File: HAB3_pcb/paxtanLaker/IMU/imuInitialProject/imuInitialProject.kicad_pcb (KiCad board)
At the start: 2 copper layers, 12 parts, among them J1 Conn_01x09_Female, J2 Conn_01x02_Female, U1 LSM9DS0

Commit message: started tracing
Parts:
- moved C3 20.4 mm to (167.6, 88.6)
- moved U1 19.2 mm to (166.4, 83.8)
- moved C1 19.2 mm to (171.4, 81.3)
- moved R2 19.2 mm to (171.4, 85.1)
- moved C2 19.2 mm to (171.4, 82.5)
- moved R4 19.2 mm to (171.4, 83.8)
- moved J2 16.7 mm to (160.0, 69.8)
- moved D1 14.5 mm to (151.1, 69.8)
- moved D2 14.5 mm to (151.1, 68.6)
- moved R1 14.5 mm to (151.1, 67.3)
- moved R3 14.5 mm to (151.1, 71.1)
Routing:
- net Net-(C1-Pad1): track 0.00 -> 38.1 mm
- net Net-(J1-Pad9): track 0.00 -> 36.8 mm
- net Net-(J1-Pad8): track 0.00 -> 30.3 mm
- net Net-(C1-Pad2): track 0.00 -> 23.7 mm
- net Net-(C3-Pad2): track 0.00 -> 4.95 mm
- net Net-(C3-Pad1): track 0.00 -> 4.50 mm
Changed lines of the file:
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@@
   (general
     (thickness 1.6)
-    (drawings 4)
-    (tracks 0)
+    (drawings 6)
+    (tracks 49)
     (zones 0)
     (modules 12)
@@
   )
   (module Capacitor_SMD:C_0402_1005Metric (layer F.Cu)
-    (at 152.4 78.74)
+    (at 171.45 81.28)
     (descr "Capacitor SMD 0402 (1005 Metric), square (rectangular) end terminal, IPC_7351 nominal, (Body size source: http://www.tortai-tech.com/upload/download/2011102023233369053.pdf), generated with kicad-footprint-generator")
     (tags capacitor)
@@
   )
   (module Capacitor_SMD:C_0402_1005Metric (layer F.Cu)
-    (at 152.4 80.01)
+    (at 171.45 82.55)
     (descr "Capacitor SMD 0402 (1005 Metric), square (rectangular) end terminal, IPC_7351 nominal, (Body size source: http://www.tortai-tech.com/upload/download/2011102023233369053.pdf), generated with kicad-footprint-generator")
     (tags capacitor)
@@
   )
   (module Capacitor_SMD:C_0402_1005Metric (layer F.Cu)
-    (at 147.32 86.36)
+    (at 167.64 88.646)
     (descr "Capacitor SMD 0402 (1005 Metric), square (rectangular) end terminal, IPC_7351 nominal, (Body size source: http://www.tortai-tech.com/upload/download/2011102023233369053.pdf), generated with kicad-footprint-generator")
     (tags capacitor)
@@
   )
   (module Diode_SMD:D_0402_1005Metric (layer F.Cu)
-    (at 142.24 81.28)
+    (at 151.13 69.85)
     (descr "Diode SMD 0402 (1005 Metric), square (rectangular) end terminal, IPC_7351 nominal, (Body size source: http://www.tortai-tech.com/upload/download/2011102023233369053.pdf), generated with kicad-footprint-generator")
     (tags diode)
@@
   )
   (module Diode_SMD:D_0402_1005Metric (layer F.Cu)
-    (at 142.24 80.01)
+    (at 151.13 68.58)
     (descr "Diode SMD 0402 (1005 Metric), square (rectangular) end terminal, IPC_7351 nominal, (Body size source: http://www.tortai-tech.com/upload/download/2011102023233369053.pdf), generated with kicad-footprint-generator")
     (tags diode)
@@
   )
   (module Resistor_SMD:R_0402_1005Metric (layer F.Cu)
-    (at 142.24 78.74)
+    (at 151.13 67.31)
     (descr "Resistor SMD 0402 (1005 Metric), square (rectangular) end terminal, IPC_7351 nominal, (Body size source: http://www.tortai-tech.com/upload/download/2011102023233369053.pdf), generated with kicad-footprint-generator")
     (tags resistor)
@@
   )
   (module Resistor_SMD:R_0402_1005Metric (layer F.Cu)
-    (at 152.4 82.55)
+    (at 171.45 85.09)
     (descr "Resistor SMD 0402 (1005 Metric), square (rectangular) end terminal, IPC_7351 nominal, (Body size source: http://www.tortai-tech.com/upload/download/2011102023233369053.pdf), generated with kicad-footprint-generator")
     (tags resistor)
@@
   )
   (module Resistor_SMD:R_0402_1005Metric (layer F.Cu)
-    (at 142.24 82.55)
+    (at 151.13 71.12)
     (descr "Resistor SMD 0402 (1005 Metric), square (rectangular) end terminal, IPC_7351 nominal, (Body size source: http://www.tortai-tech.com/upload/download/2011102023233369053.pdf), generated with kicad-footprint-generator")
     (tags resistor)
@@
   )
   (module Resistor_SMD:R_0402_1005Metric (layer F.Cu)
-    (at 152.4 81.28)
+    (at 171.45 83.82)
     (descr "Resistor SMD 0402 (1005 Metric), square (rectangular) end terminal, IPC_7351 nominal, (Body size source: http://www.tortai-tech.com/upload/download/2011102023233369053.pdf), generated with kicad-footprint-generator")
     (tags resistor)
@@
   )
   (module LSM9DS04:LGA-24LSM (layer F.Cu)
-    (at 147.32 81.28)
+    (at 166.37 83.82)
     (descr "<h3>LGA 4x4x1 mm 24-lead</h3><ul><li>0.5mm pitch</li><li>Pads are 0.35x0.2 mm square</li></ul><p>This package is used for:<p><ul><li>ST Micro LSM9DS0 3D accel/gyro/mag</li></ul>")
     (attr smd)
@@
   )
   (module Connector_PinHeader_2.54mm:PinHeader_1x02_P2.54mm_Horizontal (layer F.Cu)
-    (at 143.51 67.31)
+    (at 160.02 69.85)
     (descr "Through hole angled pin header, 1x02, 2.54mm pitch, 6mm pin length, single row")
     (tags "Through hole angled pin header THT 1x02 2.54mm single row")
@@
     (fp_line (start 10.55 4.35) (end 10.55 -1.8) (layer F.CrtYd) (width 0.05))
     (fp_line (start 10.55 -1.8) (end -1.8 -1.8) (layer F.CrtYd) (width 0.05))
-    (fp_text user %R (at 2.77 1.27 90) (layer F.Fab)
+    (fp_text user %R (at 2.54 1.27 90) (layer F.Fab)
       (effects (font (size 1 1) (thickness 0.15)))
     )
@@
     )
   )
+  (gr_line (start 176.53 64.77) (end 154.94 64.77) (angle 90) (layer F.Adhes) (width 0.2))
+  (gr_line (start 176.53 91.44) (end 176.53 64.77) (angle 90) (layer F.Adhes) (width 0.2))
+  (gr_line (start 154.94 91.44) (end 176.53 91.44) (angle 90) (layer F.Adhes) (width 0.2))
   (gr_line (start 154.94 64.77) (end 127 64.77) (angle 90) (layer F.Adhes) (width 0.2))
-  (gr_line (start 154.94 91.44) (end 154.94 64.77) (angle 90) (layer F.Adhes) (width 0.2))
   (gr_line (start 127 91.44) (end 154.94 91.44) (angle 90) (layer F.Adhes) (width 0.2))
   (gr_line (start 127 64.77) (end 127 91.44) (angle 90) (layer F.Adhes) (width 0.2))
+  (segment (start 167.155 88.646) (end 165.608 88.646) (width 0.25) (layer F.Cu) (net 1) (status 400000))
+  (segment (start 165.62 88.634) (end 165.62 85.695) (width 0.25) (layer F.Cu) (net 1) (status 800000))
+  (segment (start 165.608 88.646) (end 165.62 88.634) (width 0.25) (layer F.Cu) (net 1))
+  (segment (start 168.125 88.646) (end 168.125 87.907) (width 0.25) (layer F.Cu) (net 2) (status 400000))
+  (segment (start 166.12 87.88) (end 166.12 85.695) (width 0.25) (layer F.Cu) (net 2) (status 800000))
+  (segment (start 166.116 87.884) (end 166.12 87.88) (width 0.25) (layer F.Cu) (net 2))
+  (segment (start 168.102 87.884) (end 166.116 87.884) (width 0.25) (layer F.Cu) (net 2))
+  (segment (start 168.125 87.907) (end 168.102 87.884) (width 0.25) (layer F.Cu) (net 2))
+  (segment (start 138.685001 85.595001) (end 141.221001 85.595001) (width 0.25) (layer B.Cu) (net 12) (status 400000))
+  (segment (start 167.132 87.122) (end 167.132 85.852) (width 0.25) (layer B.Cu) (net 12))
+  (segment (start 142.748 87.122) (end 167.132 87.122) (width 0.25) (layer B.Cu) (net 12))
+  (segment (start 141.221001 85.595001) (end 142.748 87.122) (width 0.25) (layer B.Cu) (net 12))
+  (segment (start 166.62 85.695) (end 166.62 87.372) (width 0.25) (layer F.Cu) (net 13) (status 400000))
+  (segment (start 163.319001 88.135001) (end 138.685001 88.135001) (width 0.25) (layer F.Cu) (net 13) (status 800000))
+  (segment (start 164.592 89.408) (end 163.319001 88.135001) (width 0.25) (layer F.Cu) (net 13))
+  (segment (start 168.91 89.408) (end 164.592 89.408) (width 0.25) (layer F.Cu) (net 13))
+  (segment (start 168.91 87.376) (end 168.91 89.408) (width 0.25) (layer F.Cu) (net 13))
+  (segment (start 166.62 87.372) (end 166.624 87.376) (width 0.25) (layer F.Cu) (net 13))
+  (segment (start 166.624 87.376) (end 168.91 87.376) (width 0.25) (layer F.Cu) (net 13))
+  (segment (start 160.02 72.39) (end 157.226 72.39) (width 0.25) (layer B.Cu) (net 16) (status 400000))
+  (segment (start 164.592 86.36) (end 165.1 85.852) (width 0.25) (layer B.Cu) (net 16))
+  (segment (start 162.306 86.36) (end 164.592 86.36) (width 0.25) (layer B.Cu) (net 16))
+  (segment (start 161.798 85.852) (end 162.306 86.36) (width 0.25) (layer B.Cu) (net 16))
+  (segment (start 161.798 80.518) (end 161.798 82.55) (width 0.25) (layer B.Cu) (net 16))
+  (segment (start 161.798 82.55) (end 161.798 83.058) (width 0.25) (layer B.Cu) (net 16))
+  (segment (start 161.798 83.058) (end 161.798 83.312) (width 0.25) (layer B.Cu) (net 16))
+  (segment (start 161.798 83.312) (end 161.798 83.566) (width 0.25) (layer B.Cu) (net 16))
+  (segment (start 161.798 83.566) (end 161.798 83.82) (width 0.25) (layer B.Cu) (net 16))
+  (segment (start 161.798 83.82) (end 161.798 84.074) (width 0.25) (layer B.Cu) (net 16))
+  (segment (start 161.798 84.074) (end 161.798 84.582) (width 0.25) (layer B.Cu) (net 16))
+  (segment (start 161.798 84.582) (end 161.798 85.09) (width 0.25) (layer B.Cu) (net 16))
+  (segment (start 161.798 85.09) (end 161.798 85.852) (width 0.25) (layer B.Cu) (net 16))
+  (segment (start 157.226 75.946) (end 161.798 80.518) (width 0.25) (layer B.Cu) (net 16))
+  (segment (start 157.226 72.39) (end 157.226 75.946) (width 0.25) (layer B.Cu) (net 16))
+  (segment (start 161.798 85.09) (end 164.338 85.09) (width 0.25) (layer B.Cu) (net 16))
+  (segment (start 161.798 84.582) (end 164.592 84.582) (width 0.25) (layer B.Cu) (net 16))
+  (segment (start 161.798 84.074) (end 164.592 84.074) (width 0.25) (layer B.Cu) (net 16))
+  (segment (start 161.798 83.566) (end 164.338 83.566) (width 0.25) (layer B.Cu) (net 16))
+  (segment (start 161.798 83.058) (end 164.592 83.058) (width 0.25) (layer B.Cu) (net 16))
+  (segment (start 161.798 82.55) (end 164.592 82.55) (width 0.25) (layer B.Cu) (net 16))
+  (segment (start 160.02 69.85) (end 156.718 69.85) (width 0.25) (layer B.Cu) (net 17) (status 400000))
+  (segment (start 148.336 67.31) (end 150.622 67.31) (width 0.25) (layer B.Cu) (net 17))
+  (segment (start 148.336 65.786) (end 148.336 67.31) (width 0.25) (layer B.Cu) (net 17))
+  (segment (start 153.67 65.786) (end 148.336 65.786) (width 0.25) (layer B.Cu) (net 17))
+  (segment (start 156.718 69.85) (end 153.67 66.802) (width 0.25) (layer B.Cu) (net 17))
+  (segment (start 153.67 66.802) (end 153.67 65.786) (width 0.25) (layer B.Cu) (net 17))
+  (segment (start 148.336 67.31) (end 148.336 70.866) (width 0.25) (layer B.Cu) (net 17))
+  (segment (start 148.59 71.12) (end 150.622 71.12) (width 0.25) (layer B.Cu) (net 17))
+  (segment (start 148.336 70.866) (end 148.59 71.12) (width 0.25) (layer B.Cu) (net 17))
 )

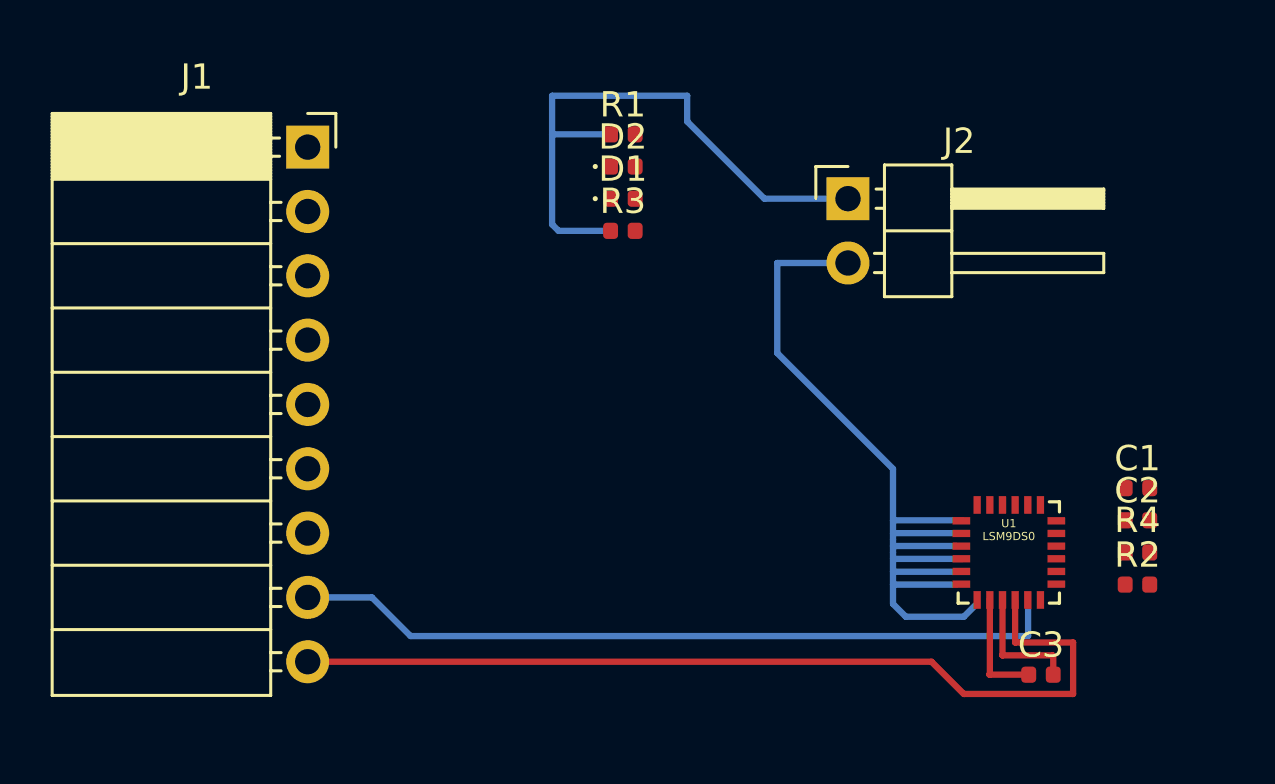
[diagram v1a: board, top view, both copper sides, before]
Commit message: Final PCB IMU
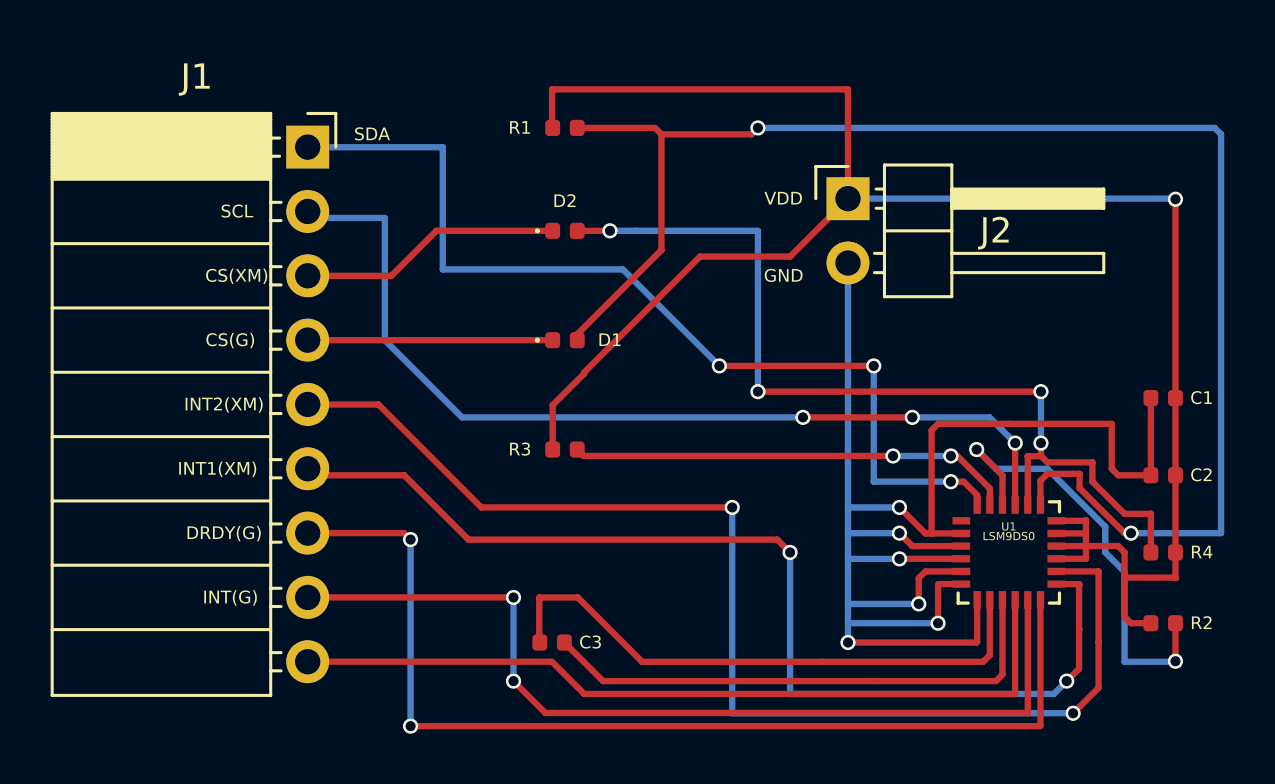
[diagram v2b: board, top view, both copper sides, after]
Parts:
- moved C3 19.3 mm to (148.3, 87.4)
- moved R3 8.93 mm to (148.8, 79.8)
- moved D1 6.04 mm to (148.8, 75.4)
- moved C1 3.70 mm to (172.5, 77.7)
- moved D2 3.42 mm to (148.8, 71.1)
- moved R1 2.30 mm to (148.8, 67.1)
- moved C2 2.05 mm to (172.5, 80.8)
- moved R2 1.83 mm to (172.5, 86.6)
- moved R4 1.02 mm to (172.5, 83.8)
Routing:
- net Net-(D1-Pad2): track 0.00 -> 60.5 mm, vias 0 -> 2
- net Net-(C1-Pad2): track 23.7 -> 75.9 mm, vias 0 -> 1
- net Net-(J1-Pad5): track 0.00 -> 47.8 mm, vias 0 -> 2
- net Net-(J1-Pad6): track 0.00 -> 42.1 mm, vias 0 -> 2
- net Net-(J1-Pad7): track 0.00 -> 41.4 mm, vias 0 -> 2
- net Net-(J1-Pad1): track 0.00 -> 38.0 mm, vias 0 -> 3
- net Net-(J1-Pad2): track 0.00 -> 37.0 mm, vias 0 -> 3
- net Net-(D2-Pad2): track 0.00 -> 37.0 mm, vias 0 -> 4
- net Net-(C1-Pad1): track 38.1 -> 65.2 mm, vias 0 -> 6
- net Net-(C3-Pad1): track 4.50 -> 22.9 mm
- net Net-(R2-Pad2): track 0.00 -> 18.2 mm, vias 0 -> 2
- net Net-(R3-Pad2): track 0.00 -> 17.6 mm, vias 0 -> 2
- net Net-(C3-Pad2): track 4.95 -> 21.0 mm
- net Net-(D2-Pad1): track 0.00 -> 10.4 mm
- net Net-(D1-Pad1): track 0.00 -> 9.68 mm
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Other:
- copper layers 2 -> 4
- net class Default: via_dia 0.8 -> 0.6
- board text added: "CS(G)"
- board text added: "CS(XM)"
- board text added: "DEN(G)"
- board text added: "DRDY(G)"
- board text added: "GND"
- board text added: "INT(G)"
- board text added: "INT1(XM)"
- board text added: "INT2(XM)"
- board text added: "SCL"
- board text added: "SDA"
- board text added: "VDD"
